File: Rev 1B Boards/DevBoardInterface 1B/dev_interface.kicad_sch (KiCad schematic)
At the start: 21 parts, among them U10 ADS1014IDGS, U6 ISO164xB, U7 ADS1014IDGS, U8 TLV9301xDBV, U9 DAC53401

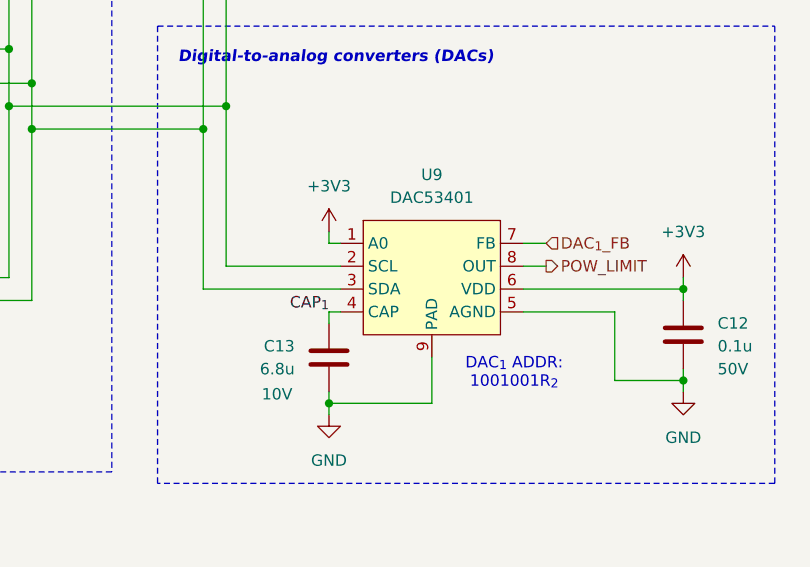
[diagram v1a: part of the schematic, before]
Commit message: Complete dev board interface layout
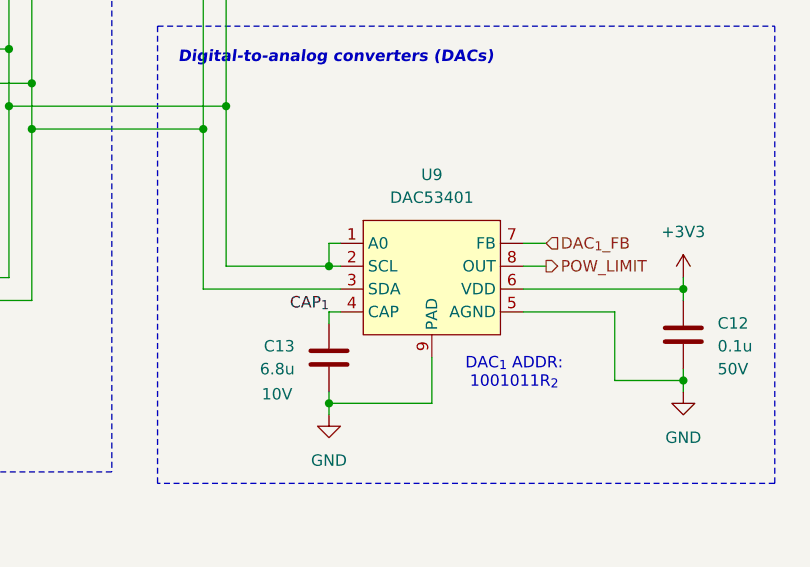
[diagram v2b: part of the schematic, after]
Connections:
- net +3V3: no longer U9.1 (A0)
- net SCL_{INT}: now also U9.1 (A0)
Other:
- note added: "DAC_{1} ADDR: 1001011R_{2}"
- note removed: "DAC_{1} ADDR: 1001001R_{2}"
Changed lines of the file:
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@@
 		)
 	)
-	(text "DAC_{1} ADDR:\n1001001R_{2}"
+	(text "DAC_{1} ADDR:\n1001011R_{2}"
 		(exclude_from_sim no)
 		(at 208.534 128.27 0)
@@
 	)
 	(junction
+		(at 187.96 118.11)
+		(diameter 0)
+		(color 0 0 0 0)
+	)
+	(junction
 		(at 187.96 133.35)
 		(diameter 0)
@@
 	(wire
 		(pts
-			(xy 187.96 114.3) (xy 187.96 115.57)
-		)
-		(stroke
-			(width 0)
-			(type default)
-		)
-	)
-	(wire
-		(pts
 			(xy 205.74 71.12) (xy 238.76 71.12)
 		)
@@
 	(wire
 		(pts
+			(xy 187.96 118.11) (xy 189.23 118.11)
+		)
+		(stroke
+			(width 0)
+			(type default)
+		)
+	)
+	(wire
+		(pts
 			(xy 147.32 97.79) (xy 154.94 97.79)
 		)
@@
 	(wire
 		(pts
-			(xy 176.53 118.11) (xy 189.23 118.11)
+			(xy 176.53 118.11) (xy 187.96 118.11)
 		)
 		(stroke
@@
 	(wire
 		(pts
+			(xy 187.96 115.57) (xy 187.96 118.11)
+		)
+		(stroke
+			(width 0)
+			(type default)
+		)
+	)
+	(wire
+		(pts
 			(xy 176.53 71.12) (xy 176.53 100.33)
 		)
@@
 					(unit 1)
 				)
-			)
-		)
-	)
-	(symbol
-		(lib_id "power:+3V3")
-		(at 187.96 114.3 0)
-		(mirror y)
-		(unit 1)
-		(exclude_from_sim no)
-		(in_bom yes)
-		(on_board yes)
-		(dnp no)
-		(fields_autoplaced yes)
-		(property "Reference" "#PWR071"
-			(at 187.96 118.11 0)
-			(effects
-				(font
-					(size 1.27 1.27)
-				)
-				(hide yes)
-			)
-		)
-		(property "Value" "+3V3"
-			(at 187.96 109.22 0)
-			(effects
-				(font
-					(size 1.27 1.27)
-				)
-			)
-		)
-		(property "Footprint" ""
-			(at 187.96 114.3 0)
-			(effects
-				(font
-					(size 1.27 1.27)
-				)
-				(hide yes)
-			)
-		)
-		(property "Datasheet" ""
-			(at 187.96 114.3 0)
-			(effects
-				(font
-					(size 1.27 1.27)
-				)
-				(hide yes)
-			)
-		)
-		(property "Description" "Power symbol creates a global label with name \"+3V3\""
-			(at 187.96 114.3 0)
-			(effects
-				(font
-					(size 1.27 1.27)
-				)
-				(hide yes)
-			)
-		)
-		(pin "1"
-		)
-		(instances
-			(project "DevBoardInterface 1B"
-				(path "/99fb25ed-9aca-432a-ba59-ddfa2561a3f7/c349ddf1-3671-4355-a172-174d007a1d8b"
-					(reference "#PWR071")
-					(unit 1)
-				)
